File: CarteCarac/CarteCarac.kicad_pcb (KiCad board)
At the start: 4 copper layers, 250 x 130 mm, 30 parts

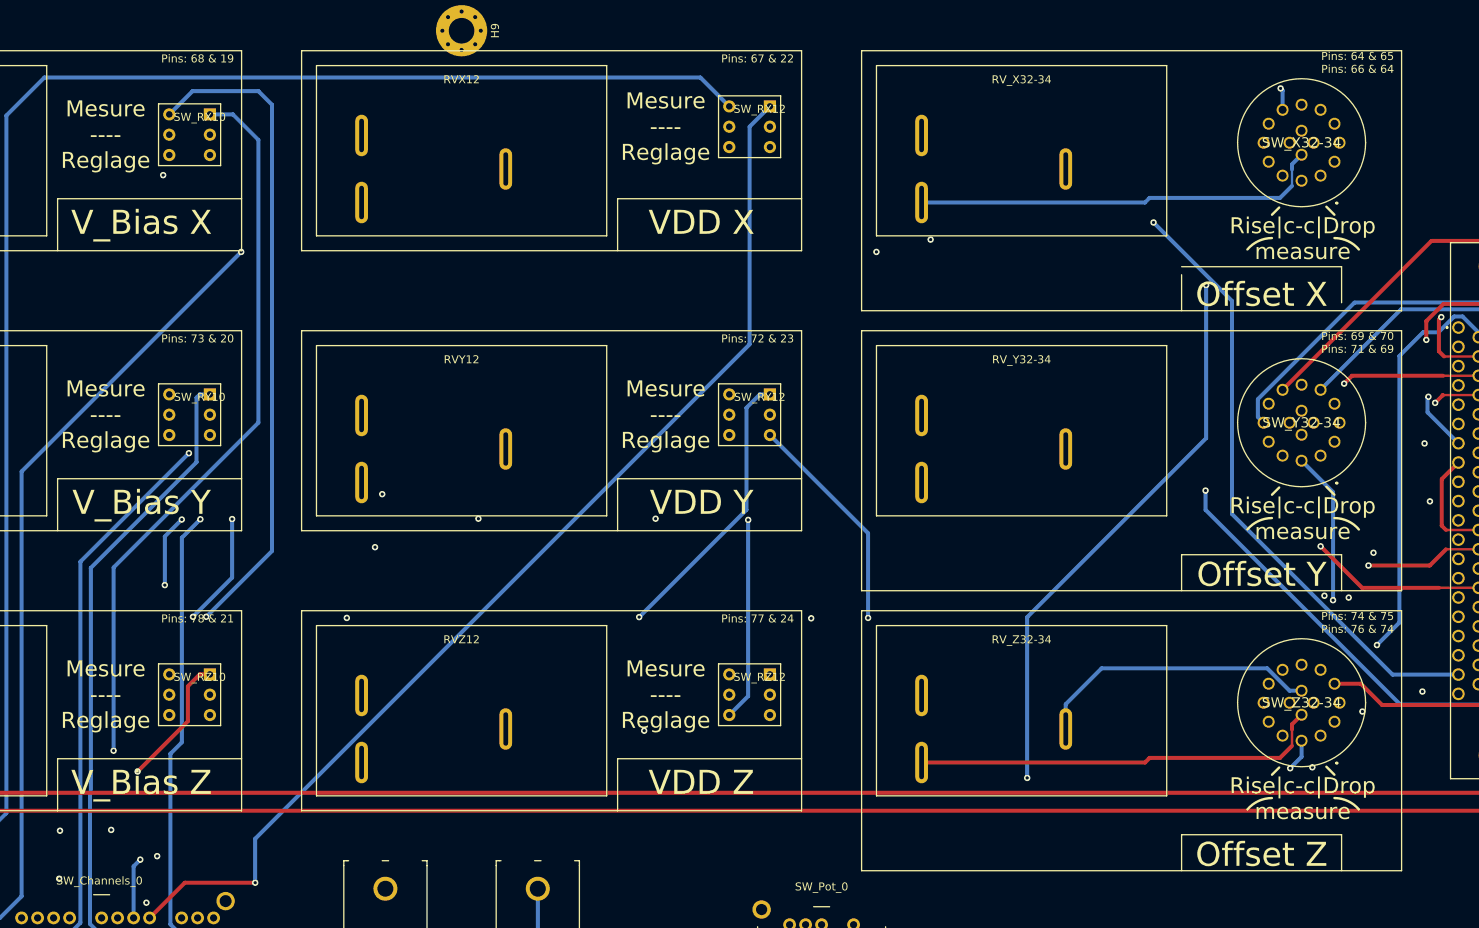
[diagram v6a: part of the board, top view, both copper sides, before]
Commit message: Correction et amélioration de la sérigraphie
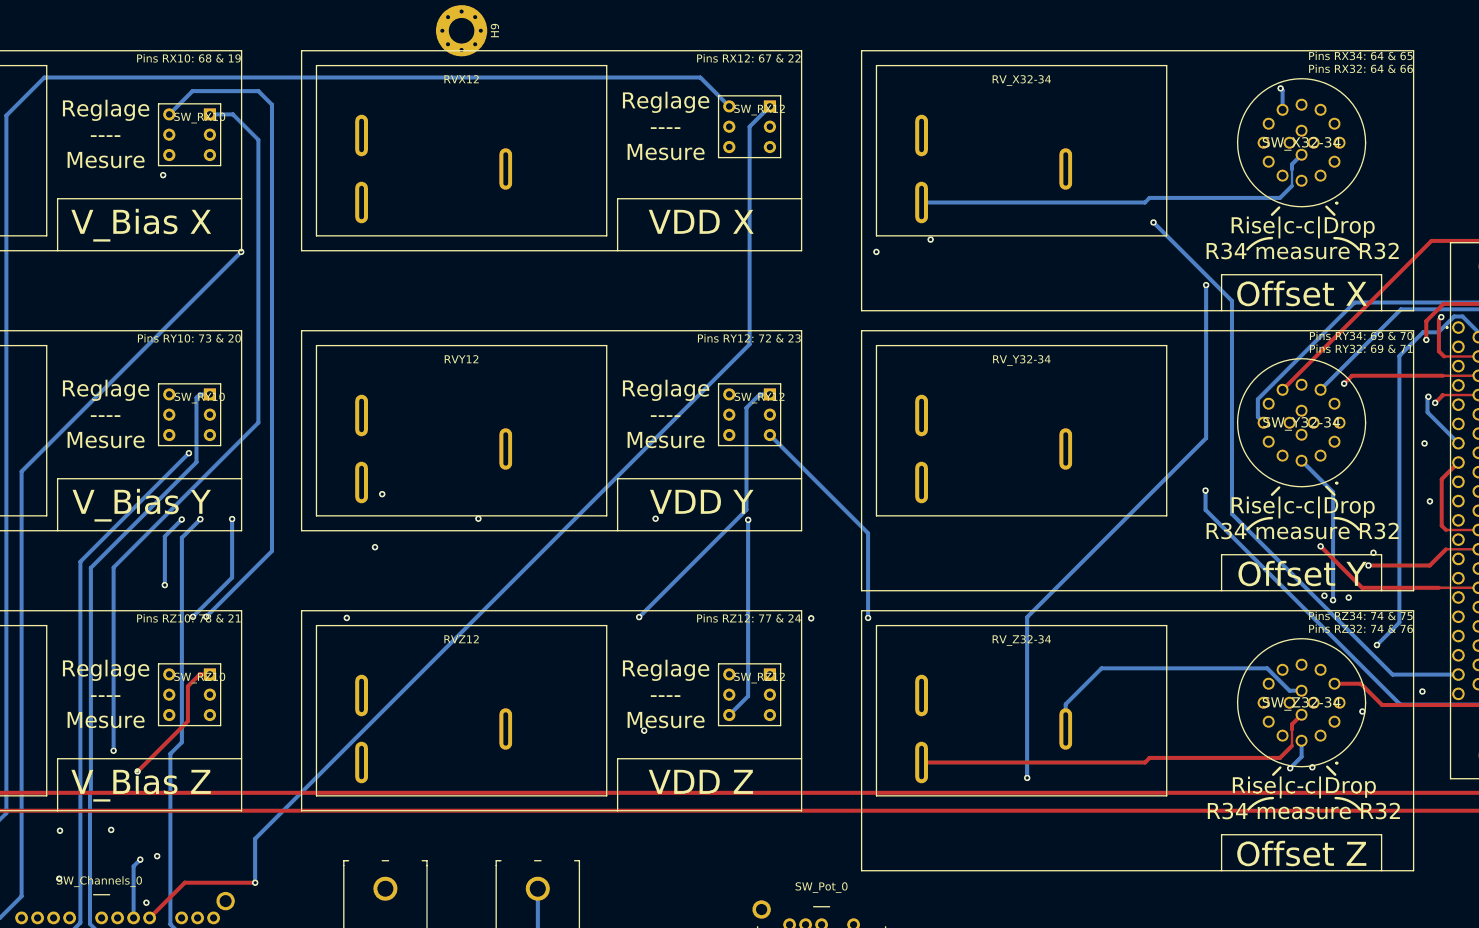
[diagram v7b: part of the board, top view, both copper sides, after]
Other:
- board text added: "Pins RX10: 68 & 19"
- board text added: "Pins RX12: 67 & 22"
- board text added: "Pins RX34: 64 & 65 Pins RX32: 64 & 66"
- board text added: "Pins RY10: 73 & 20"
- board text added: "Pins RY12: 72 & 23"
- board text added: "Pins RY34: 69 & 70 Pins RY32: 69 & 71"
- board text added: "Pins RZ10: 78 & 21"
- board text added: "Pins RZ12: 77 & 24"
- board text added: "Pins RZ34: 74 & 75 Pins RZ32: 74 & 76"
- board text added: "Reglage ---- Mesure"
- board text added: "Rise|c-c|Drop R34 measure R32"
- board text removed: "Mesure ---- Reglage"
- board text removed: "Pins: 64 & 65 Pins: 66 & 64"
- board text removed: "Pins: 67 & 22"
- board text removed: "Pins: 68 & 19"
- board text removed: "Pins: 69 & 70 Pins: 71 & 69"
- board text removed: "Pins: 72 & 23"
- board text removed: "Pins: 73 & 20"
- board text removed: "Pins: 74 & 75 Pins: 76 & 74"
- board text removed: "Pins: 77 & 24"
- board text removed: "Pins: 78 & 21"
- board text removed: "Rise|c-c|Drop measure"
